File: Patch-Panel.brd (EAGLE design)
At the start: 86.4 x 209.6 mm, 55 parts, among them J1 APPPP45_PCB_VERT, J10 APPPP45_PCB_VERT, J11 APPPP45_PCB_VERT, J12 APPPP45_PCB_VERT, J13 APPPP45_PCB_VERT, J14 APPPP45_PCB_VERT, J15 APPPP45_PCB_VERT, J16 APPPP45_PCB_VERT, J17 APPPP45_PCB_VERT, J18 APPPP45_PCB_VERT, J19 APPPP45_PCB_VERT, J2 APPPP45_PCB_VERT, J20 APPPP45_PCB_VERT, J21 APPPP45_PCB_VERT, J22 APPPP45_PCB_VERT, J23 APPPP45_PCB_VERT, J24 APPPP45_PCB_VERT, J25 APPPP45_PCB_VERT, J26 APPPP45_PCB_VERT, J27 APPPP45_PCB_VERT, J28 APPPP45_PCB_VERT, J29 APPPP45_PCB_VERT, J3 APPPP45_PCB_VERT, J30 APPPP45_PCB_VERT, J31 APPPP45_PCB_VERT, J32 APPPP45_PCB_VERT, J33 APPPP45_PCB_VERT, J34 APPPP45_PCB_VERT, J35 APPPP45_PCB_VERT, J36 APPPP45_PCB_VERT, J37 APPPP45_PCB_VERT, J38 APPPP45_PCB_VERT, J39 APPPP45_PCB_VERT, J4 APPPP45_PCB_VERT, J40 APPPP45_PCB_VERT, J41 APPPP45_PCB_VERT, J42 APPPP45_PCB_VERT, J43 APPPP45_PCB_VERT, J44 APPPP45_PCB_VERT, J45 APPPP45_PCB_VERT, J46 APPPP45_PCB_VERT, J47 APPPP45_PCB_VERT, J5 APPPP45_PCB_VERT, J6 APPPP45_PCB_VERT, J7 APPPP45_PCB_VERT, J8 APPPP45_PCB_VERT

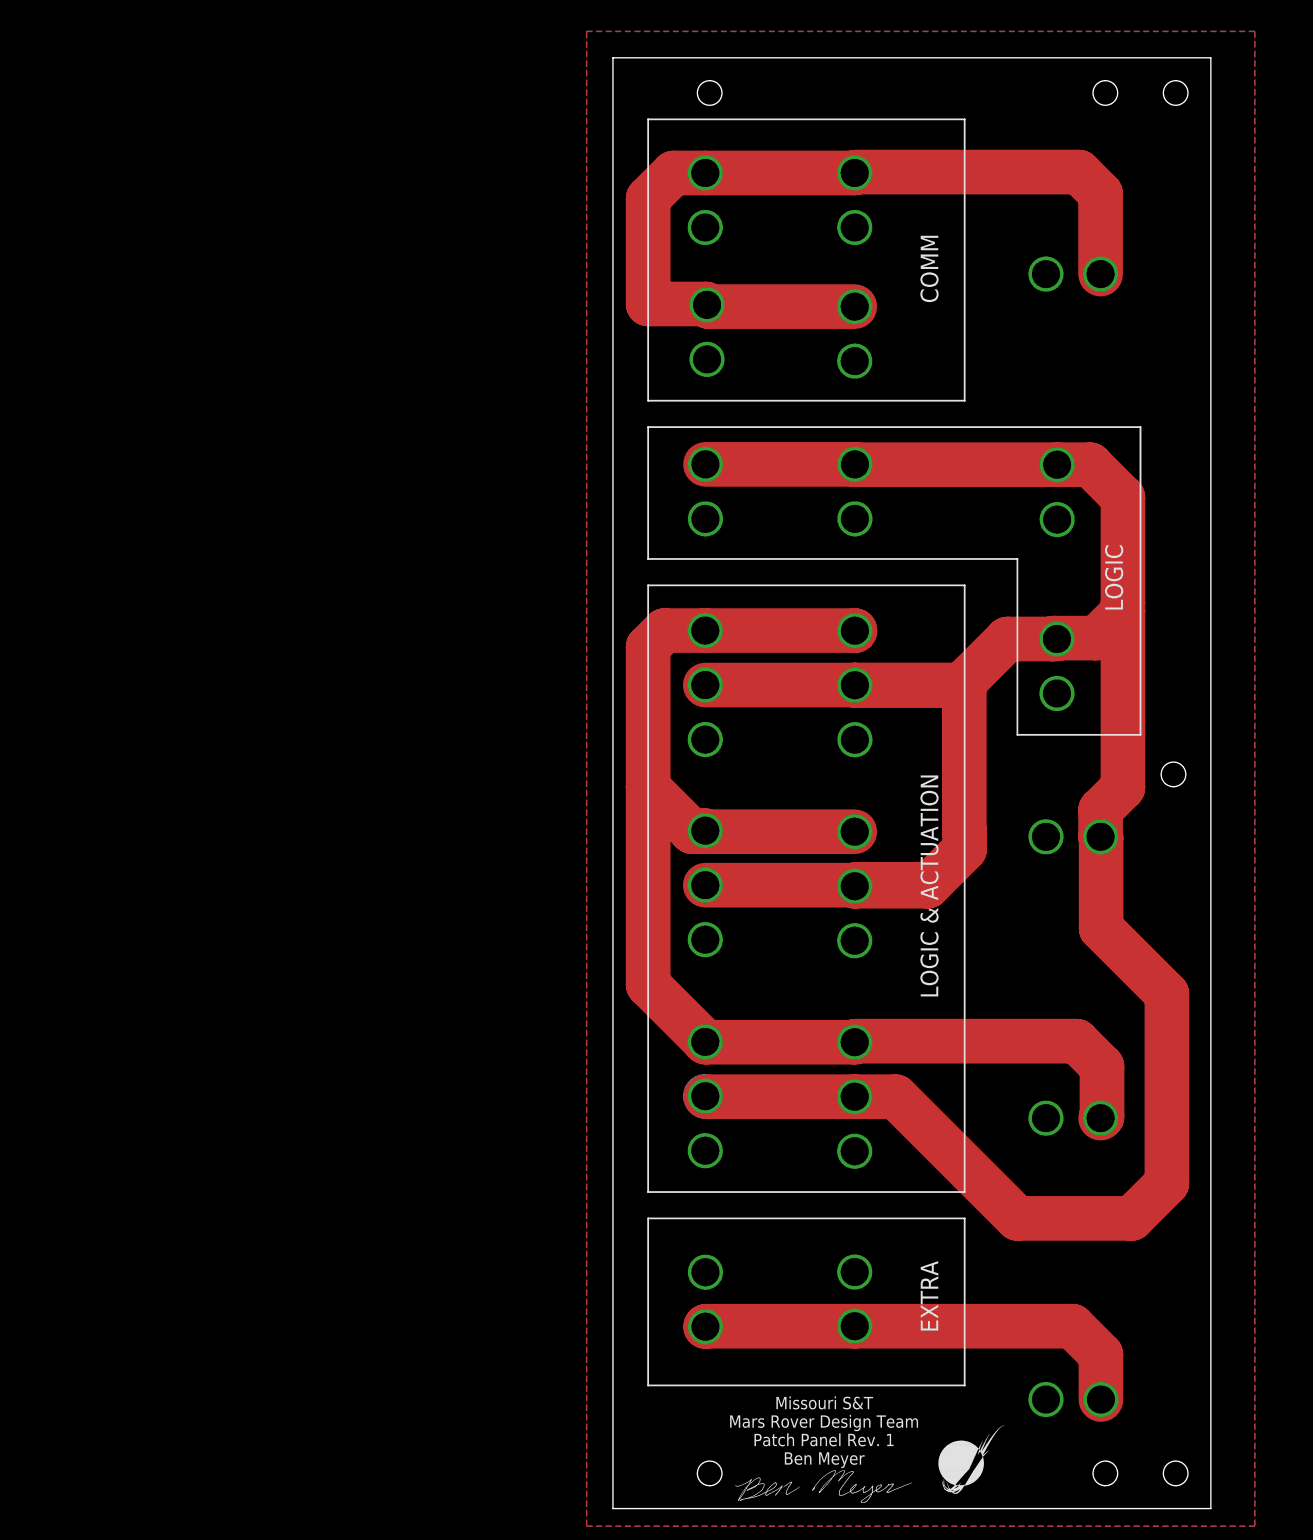
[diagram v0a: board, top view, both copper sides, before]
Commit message: Last edits before fabrication
tidied a couple traces and labels, and added a martian.
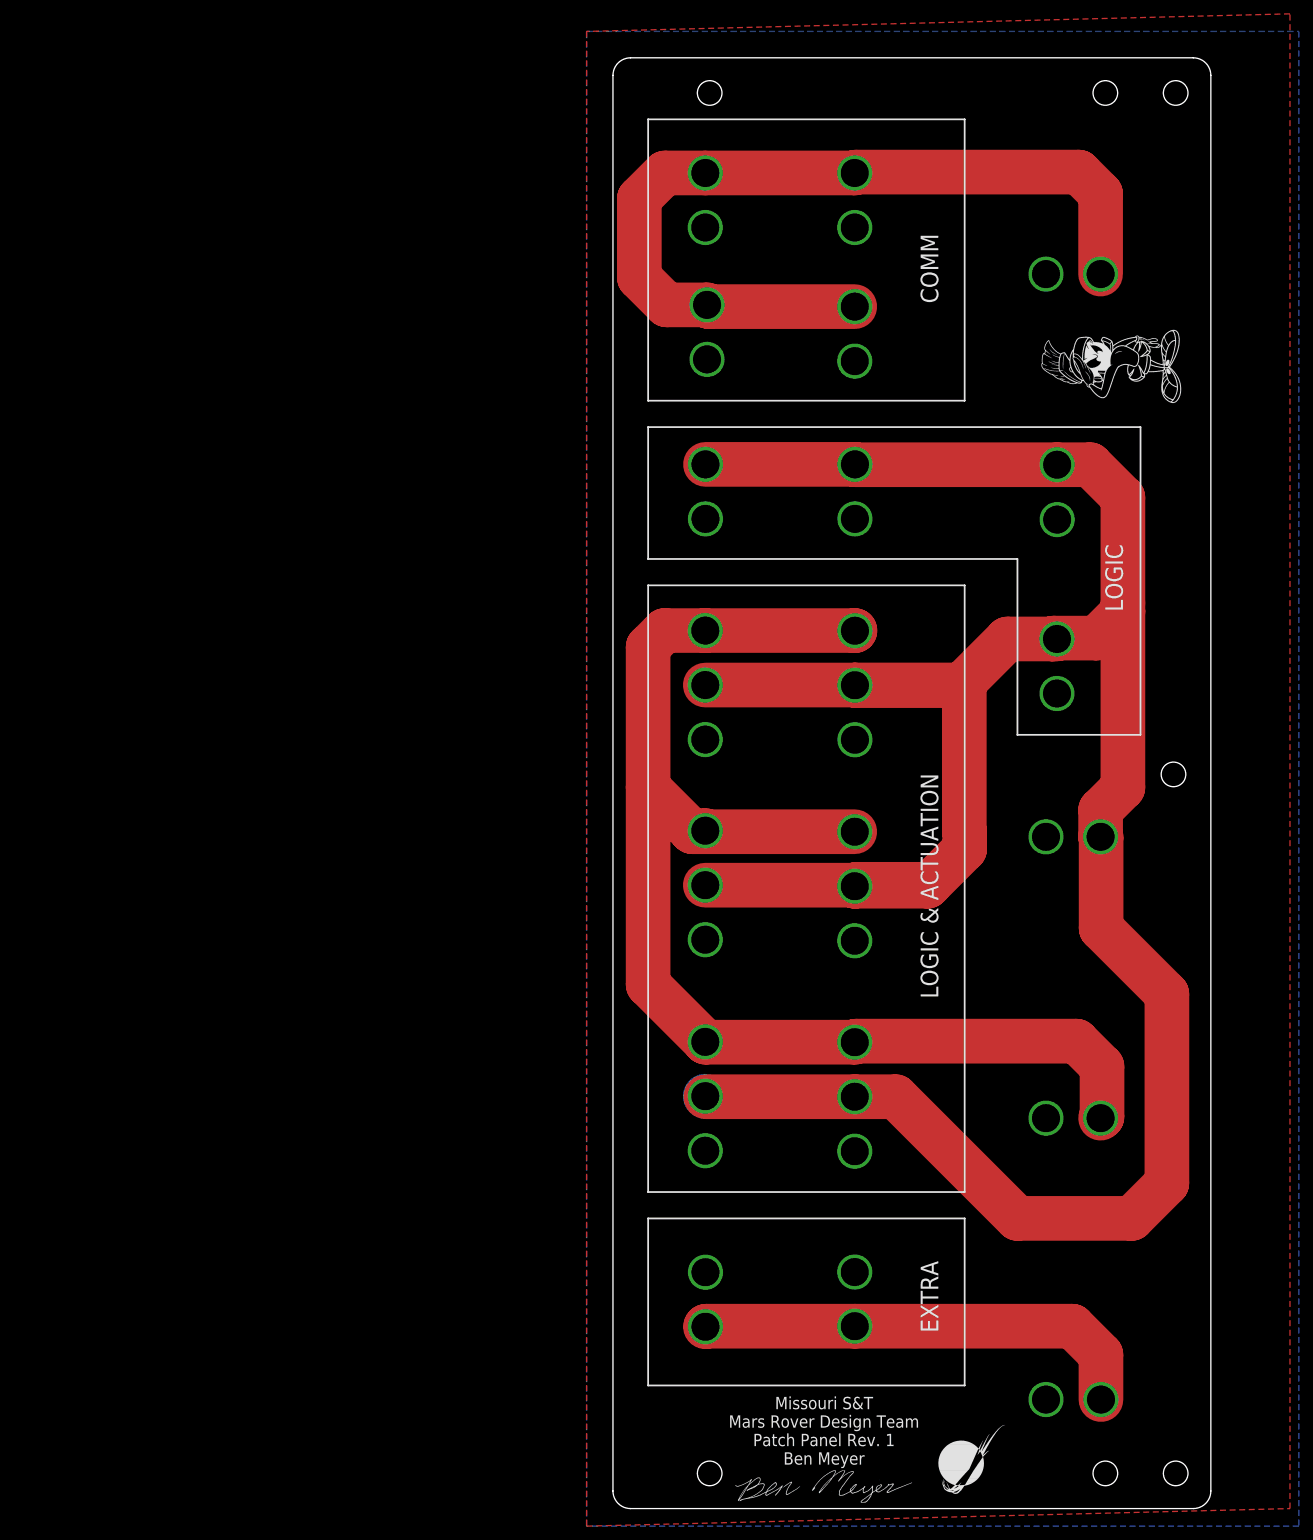
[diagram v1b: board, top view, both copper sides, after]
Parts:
- added U$2: MARVIN-THE-MARTIAN, MRDT-Hardware:MARVIN
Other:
- outline, holes or cut-outs redrawn
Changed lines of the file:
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@@
 <?xml version="1.0" encoding="utf-8"?>
 <!DOCTYPE eagle SYSTEM "eagle.dtd">
-<eagle version="7.4.0">
+<eagle version="6.5.0">
 <drawing>
 <settings>
@@
 <board>
 <plain>
-<wire x1="76.2" y1="0" x2="162.56" y2="0" width="0" layer="20"/>
-<wire x1="162.56" y1="0" x2="162.56" y2="209.55" width="0" layer="20"/>
-<wire x1="162.56" y1="209.55" x2="76.2" y2="209.55" width="0" layer="20"/>
-<wire x1="76.2" y1="209.55" x2="76.2" y2="0" width="0" layer="20"/>
+<wire x1="76.2" y1="207.01" x2="76.2" y2="2.54" width="0" layer="20"/>
+<wire x1="76.2" y1="2.54" x2="78.74" y2="0" width="0" layer="20" curve="90"/>
+<wire x1="78.74" y1="0" x2="160.02" y2="0" width="0" layer="20"/>
+<wire x1="160.02" y1="0" x2="162.56" y2="2.54" width="0" layer="20" curve="90"/>
+<wire x1="162.56" y1="2.54" x2="162.56" y2="207.01" width="0" layer="20"/>
+<wire x1="162.56" y1="207.01" x2="160.02" y2="209.55" width="0" layer="20" curve="90"/>
+<wire x1="160.02" y1="209.55" x2="78.74" y2="209.55" width="0" layer="20"/>
+<wire x1="78.74" y1="209.55" x2="76.2" y2="207.01" width="0" layer="20" curve="90"/>
 <text x="155.0416" y="174.4726" size="1.778" layer="26" rot="MR90">COMM</text>
 <text x="155.067" y="93.7006" size="1.778" layer="26" rot="MR90">LOGIC</text>
@@
 <pass name="Default">
 <param name="RoutingGrid" value="50mil"/>
-<param name="AutoGrid" value="1"/>
-<param name="Efforts" value="0"/>
-<param name="TopRouterVariant" value="1"/>
 <param name="tpViaShape" value="round"/>
-<param name="PrefDir.1" value="a"/>
+<param name="PrefDir.1" value="|"/>
 <param name="PrefDir.2" value="0"/>
 <param name="PrefDir.3" value="0"/>
@@
 <param name="PrefDir.14" value="0"/>
 <param name="PrefDir.15" value="0"/>
-<param name="PrefDir.16" value="a"/>
+<param name="PrefDir.16" value="-"/>
 <param name="cfVia" value="8"/>
 <param name="cfNonPref" value="5"/>
@@
 <element name="LOGO1" library="MRDT-Hardware" package="MRDT_LOGO" value="MRDT_LOGO" x="123.19" y="1.27"/>
 <element name="U$1" library="sig" package="BEN-MEYER-SIG" value="BEN-MEYER" x="93.6752" y="0.8382"/>
+<element name="U$2" library="MRDT-Hardware" package="MARVIN" value="MARVIN-THE-MARTIAN" x="158.75" y="158.75" rot="R90"/>
 </elements>
 <signals>
@@
 <polygon width="0.4064" layer="16">
 <vertex x="72.39" y="213.36"/>
-<vertex x="168.91" y="213.36"/>
-<vertex x="168.91" y="-2.54"/>
+<vertex x="175.26" y="213.36"/>
+<vertex x="175.26" y="-2.54"/>
 <vertex x="72.39" y="-2.54"/>
 </polygon>
 <polygon width="0.4064" layer="1">
-<vertex x="168.91" y="213.36"/>
+<vertex x="173.99" y="215.9"/>
 <vertex x="72.39" y="213.36"/>
 <vertex x="72.39" y="-2.54"/>
-<vertex x="168.91" y="-2.54"/>
+<vertex x="173.99" y="0"/>
 </polygon>
 <contactref element="J25" pad="P$1"/>
@@
 <wire x1="111.252" y1="193.04" x2="111.125" y2="192.913" width="6.4516" layer="1"/>
 <wire x1="111.125" y1="192.913" x2="89.535" y2="192.913" width="6.4516" layer="1"/>
-<wire x1="89.535" y1="192.913" x2="84.963" y2="192.913" width="6.4516" layer="1"/>
-<wire x1="84.963" y1="192.913" x2="81.28" y2="189.23" width="6.4516" layer="1"/>
-<wire x1="81.28" y1="189.23" x2="81.28" y2="173.99" width="6.4516" layer="1"/>
-<wire x1="81.28" y1="173.99" x2="89.662" y2="173.99" width="6.4516" layer="1"/>
-<wire x1="89.662" y1="173.99" x2="89.789" y2="173.863" width="6.4516" layer="1"/>
 <wire x1="111.125" y1="173.609" x2="90.043" y2="173.609" width="6.4516" layer="1"/>
 <wire x1="90.043" y1="173.609" x2="89.789" y2="173.863" width="6.4516" layer="1"/>
+<wire x1="89.535" y1="192.913" x2="83.693" y2="192.913" width="6.4516" layer="1"/>
+<wire x1="83.693" y1="192.913" x2="80.01" y2="189.23" width="6.4516" layer="1"/>
+<wire x1="89.789" y1="173.863" x2="83.947" y2="173.863" width="6.4516" layer="1"/>
+<wire x1="83.947" y1="173.863" x2="80.01" y2="177.8" width="6.4516" layer="1"/>
+<wire x1="80.01" y1="177.8" x2="80.01" y2="189.23" width="6.4516" layer="1"/>
 </signal>
 <signal name="EXT-12V">

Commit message: 2018 Patch Panel Rev1
The 12V buses are being passed to patch panel. In order from bottom of power board to top, Actuation 15A, Logic 5A, Communication 5A.  There is no extra bus this year. Add one more Logic/Act connection
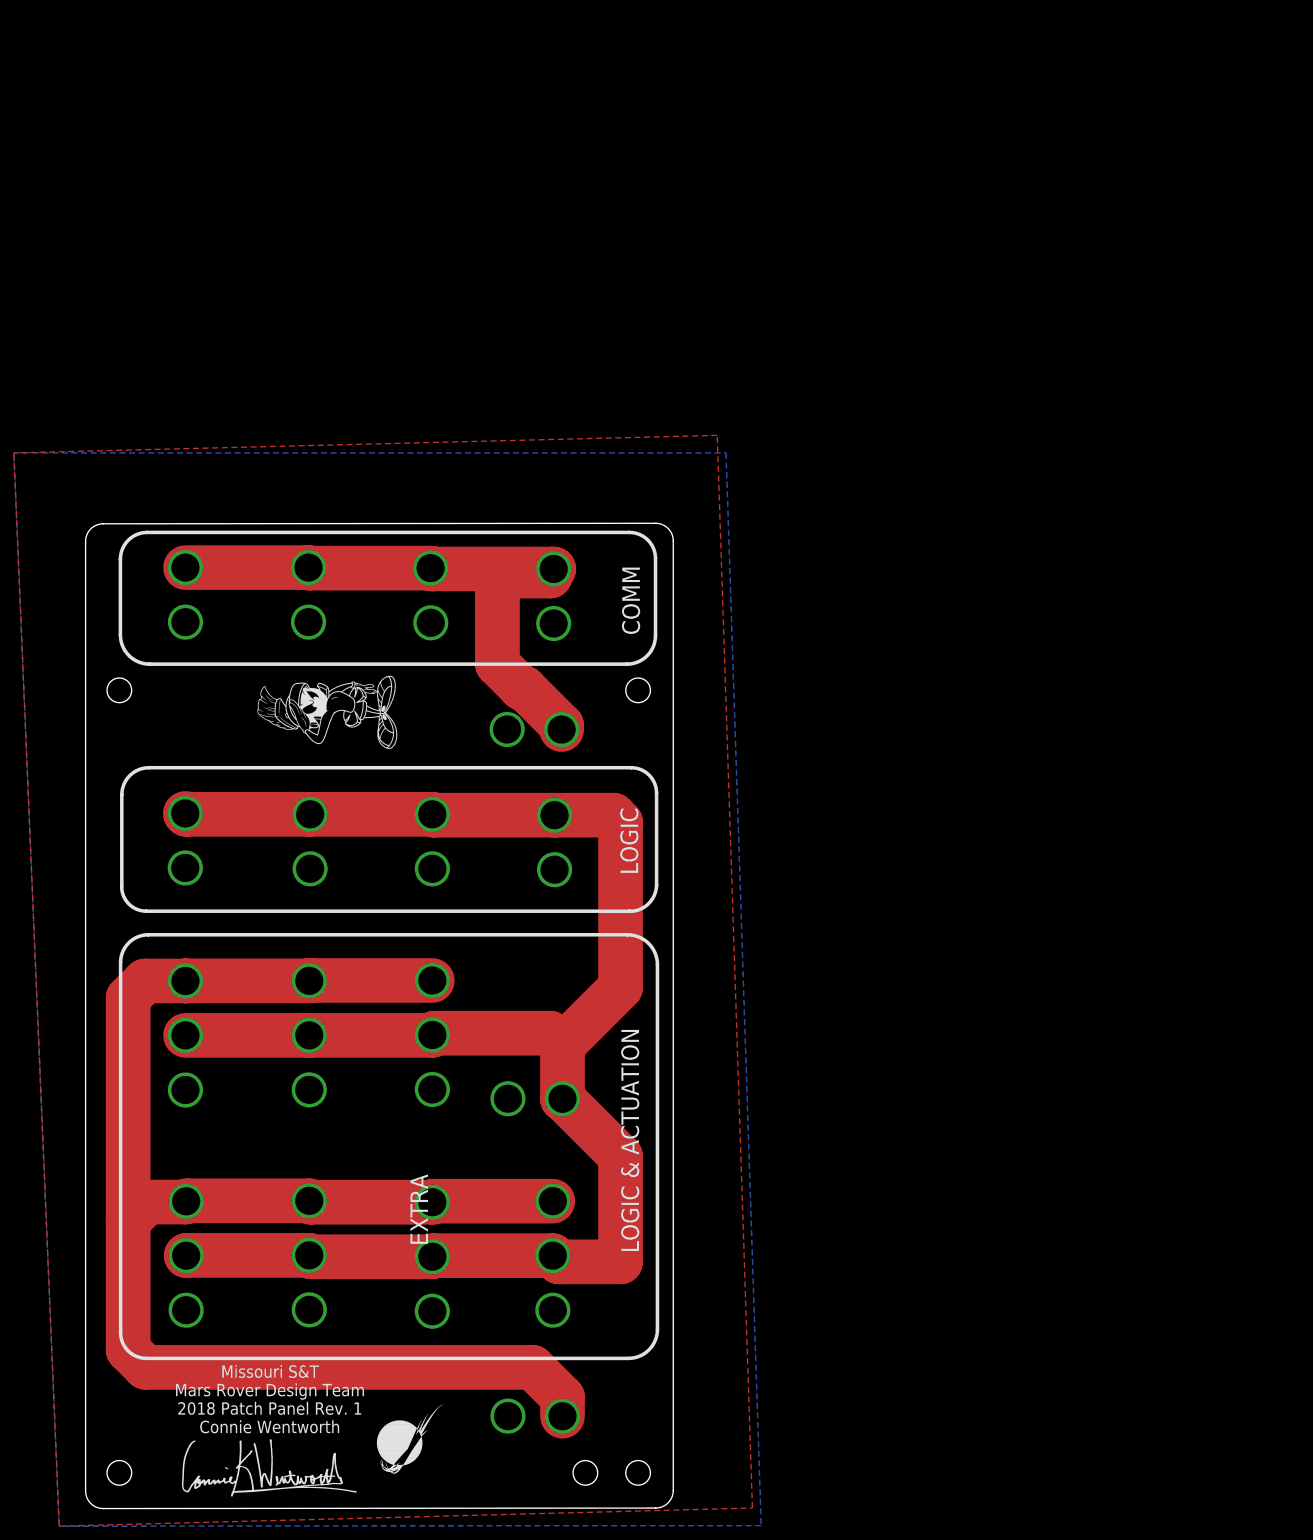
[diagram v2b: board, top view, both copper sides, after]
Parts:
- removed H1, H2: MOUNTING_HOLE#6, MRDT-Hardware:#6_SCREW
- removed J44, J45, J46, J47: APPPP45_PCB_VERT, MRDT-Connectors:APP45_PCB_VERT
- added J9: APPPP45_PCB_VERT, MRDT-Connectors:APP45_PCB_VERT
- U$1: value BEN-MEYER -> CONNIE_WENTWORTH_SIGNATURE; device sig:BEN-MEYER-SIG -> MRDT-Signatures:CONNIE_WENTWORTH_SIGNATURE
- moved J8 158.7 mm to (64.3, 40.5)
- moved J23 150.5 mm to (11.3, 72.3)
- moved U$2 123.8 mm to (45.5, 108.8)
- moved H3 121.3 mm to (4.90, 118.2)
- moved J25 119.2 mm to (11.3, 96.5)
- moved J36 119.2 mm to (11.3, 104.3)
- moved J13 110.9 mm to (46.9, 96.3)
- moved J42 110.9 mm to (46.9, 104.2)
- moved J16 109.1 mm to (11.3, 64.4)
- moved J27 109.1 mm to (11.3, 80.1)
- moved J5 103.0 mm to (64.8, 115.7), flipped to the bottom, turned to 180 degrees
- moved J4 96.2 mm to (57.0, 115.7), flipped to the bottom, turned to 180 degrees
- moved J40 93.3 mm to (29.3, 104.2)
- moved J43 93.3 mm to (29.3, 96.3)
- moved J33 91.7 mm to (46.7, 131.9)
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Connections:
- removed net EXT-12V: J44.P$1, J46.P$1, J7.P$1
- net ACT-12V: now also J9.P$1
- net COM-12V: now also J28.P$1, J30.P$1, J32.P$1, J34.P$1; no longer J36.P$1, J38.P$1, J40.P$1, J42.P$1
- net GND: now also J7.P$1; no longer J45.P$1, J47.P$1, J8.P$1
- net LOG-12V: now also J36.P$1, J38.P$1, J40.P$1, J42.P$1, J8.P$1; no longer J28.P$1, J30.P$1, J32.P$1, J34.P$1
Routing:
- net LOG-12V: track 398.4 -> 252.5 mm, vias 1 -> 0
- net EXT-12V: track 65.3 -> 0.00 mm
- net COM-12V: track 125.4 -> 88.4 mm
- net ACT-12V: track 192.5 -> 226.8 mm
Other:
- board size 86.4 x 209.6 mm -> 84.9 x 142.3 mm
- board text added: "Missouri S&T Mars Rover Design Team 2018 Patch Panel Rev. 1 Connie Wentworth"
- board text removed: "Missouri S&T Mars Rover Design Team Patch Panel Rev. 1 Ben Meyer"
